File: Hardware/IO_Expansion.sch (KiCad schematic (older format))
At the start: 59 parts, among them J10 IO_Power, J12 Screw_Terminal_01x02, J13 Screw_Terminal_01x02, J16 Screw_Terminal_01x02, J17 Screw_Terminal_01x02, U12 MCP23017_SO, U13 APM4953, U21 LM317_TO-252, U22 6N137, U23 6N137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

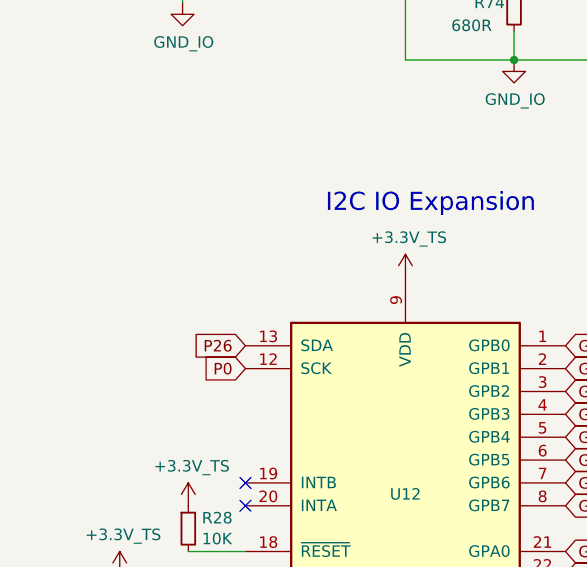
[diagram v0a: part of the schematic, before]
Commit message: fixed silk screen issues with rev_1
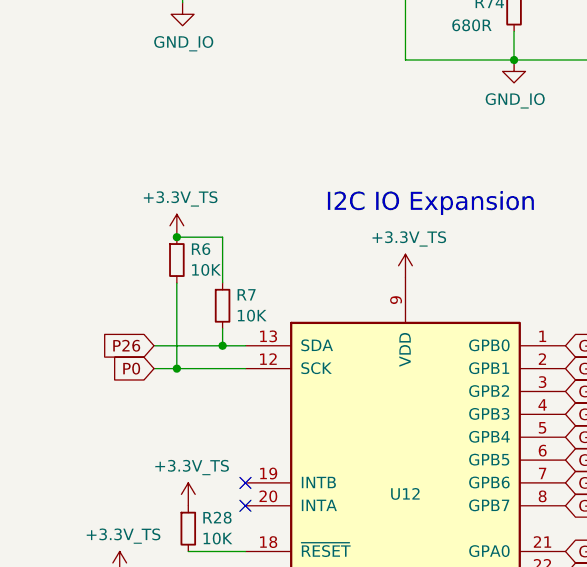
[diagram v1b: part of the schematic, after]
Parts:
- added R6, R7: 10K, Resistor_SMD:R_0603_1608Metric, symbol Device:R_Small
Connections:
- net +3V3_TS: now also R6.1, R7.1
- net P0: now also R6.2
- net P26: now also R7.2
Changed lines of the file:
@@
 	1    0    0    -1
 $EndComp
-Text GLabel 1450 3375 0    50   Input ~ 0
+Text GLabel 1050 3375 0    50   Input ~ 0
 P26
-Text GLabel 1450 3475 0    50   Input ~ 0
+Text GLabel 1050 3475 0    50   Input ~ 0
 P0
 Text Notes 1800 2800 0    79   ~ 0
@@
 	0    -1   -1   0
 $EndComp
+$Comp
+L Device:R_Small R?
+U 1 1 6047BDF6
+P 1350 3200
+AR Path="/6047BDF6" Ref="R?"  Part="1"
+AR Path="/6017311C/6047BDF6" Ref="R7"  Part="1"
+F 0 "R7" H 1409 3246 50  0000 L CNN
+F 1 "10K" H 1409 3155 50  0000 L CNN
+F 2 "Resistor_SMD:R_0603_1608Metric" H 1350 3200 50  0001 C CNN
+F 3 "https://datasheet.lcsc.com/szlcsc/Uniroyal-Elec-0603WAF1002T5E_C25804.pdf" H 1350 3200 50  0001 C CNN
+F 4 "C25804" H 1350 3200 50  0001 C CNN "LCSC"
+F 5 "BASIC" H 1350 3200 50  0001 C CNN "Type"
+	1    1350 3200
+	1    0    0    -1
+$EndComp
+$Comp
+L Device:R_Small R?
+U 1 1 6047C966
+P 1150 3000
+AR Path="/6047C966" Ref="R?"  Part="1"
+AR Path="/6017311C/6047C966" Ref="R6"  Part="1"
+F 0 "R6" H 1209 3046 50  0000 L CNN
+F 1 "10K" H 1209 2955 50  0000 L CNN
+F 2 "Resistor_SMD:R_0603_1608Metric" H 1150 3000 50  0001 C CNN
+F 3 "https://datasheet.lcsc.com/szlcsc/Uniroyal-Elec-0603WAF1002T5E_C25804.pdf" H 1150 3000 50  0001 C CNN
+F 4 "C25804" H 1150 3000 50  0001 C CNN "LCSC"
+F 5 "BASIC" H 1150 3000 50  0001 C CNN "Type"
+	1    1150 3000
+	1    0    0    -1
+$EndComp
+$Comp
+L Tensile_Board:+3.3V_TS #PWR0111
+U 1 1 6047D0EA
+P 1150 2900
+F 0 "#PWR0111" H 1150 2750 50  0001 C CNN
+F 1 "+3.3V_TS" H 1165 3073 50  0000 C CNN
+F 2 "" H 1150 2900 50  0001 C CNN
+F 3 "" H 1150 2900 50  0001 C CNN
+	1    1150 2900
+	1    0    0    -1
+$EndComp
+Wire Wire Line
+	1150 2900 1350 2900
+Wire Wire Line
+	1350 2900 1350 3100
+Connection ~ 1150 2900
+Wire Wire Line
+	1350 3300 1350 3375
+Wire Wire Line
+	1350 3375 1450 3375
+Wire Wire Line
+	1150 3100 1150 3475
+Wire Wire Line
+	1150 3475 1450 3475
+Wire Wire Line
+	1150 3475 1050 3475
+Connection ~ 1150 3475
+Wire Wire Line
+	1050 3375 1350 3375
+Connection ~ 1350 3375
 $EndSCHEMATC
